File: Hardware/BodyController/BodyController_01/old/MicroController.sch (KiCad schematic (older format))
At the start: 18 parts, among them SW1 PTS645SM43SMTR92 LFS, U1 PIC33EPxxxMU810, Y1 8MHz

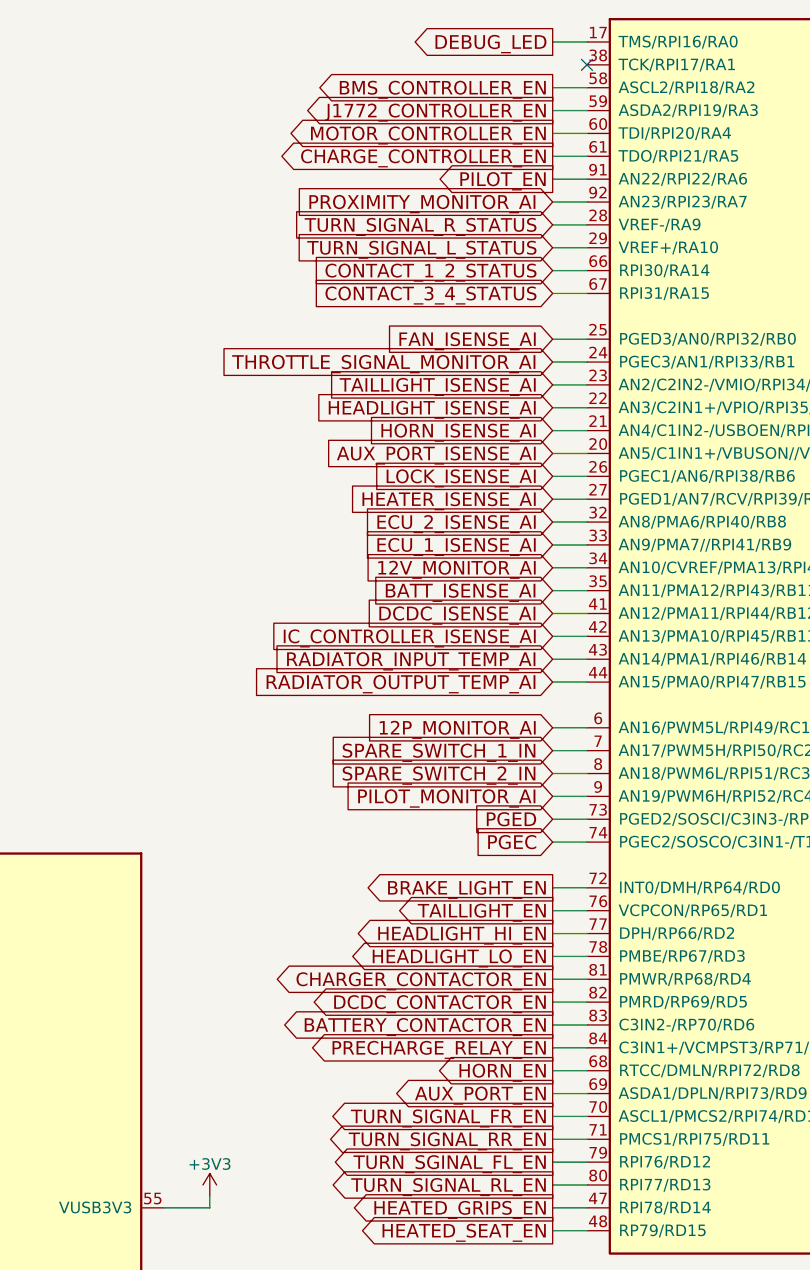
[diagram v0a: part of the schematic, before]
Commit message: Final layout for real this time. larger vias for EuroCircuit minimum rule.
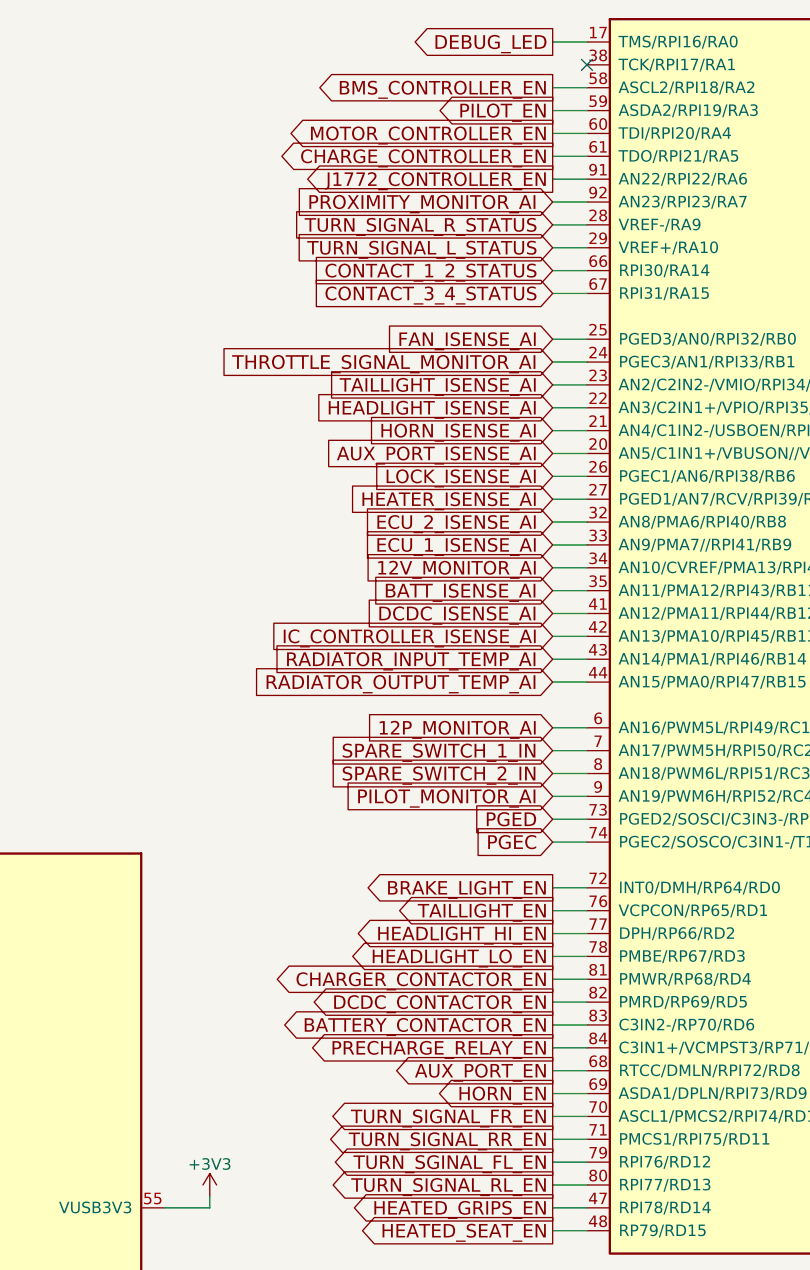
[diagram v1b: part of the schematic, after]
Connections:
- net AUX_PORT_EN: now also U1.68 (RTCC/DMLN/RPI72/RD8); no longer U1.69 (ASDA1/DPLN/RPI73/RD9)
- net HORN_EN: now also U1.69 (ASDA1/DPLN/RPI73/RD9); no longer U1.68 (RTCC/DMLN/RPI72/RD8)
- net J1772_CONTROLLER_EN: now also U1.91 (AN22/RPI22/RA6); no longer U1.59 (ASDA2/RPI19/RA3)
- net PILOT_EN: now also U1.59 (ASDA2/RPI19/RA3); no longer U1.91 (AN22/RPI22/RA6)
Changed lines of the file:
@@
 Text GLabel 5600 3000 0    59   Input ~ 0
 12V_MONITOR_AI
-Text GLabel 5600 5300 0    59   Output ~ 0
+Text GLabel 5600 5200 0    59   Output ~ 0
 AUX_PORT_EN
 Text GLabel 5600 4600 0    59   Output ~ 0
@@
 Text GLabel 5600 2200 0    59   Input ~ 0
 TAILLIGHT_ISENSE_AI
-Text GLabel 5600 5200 0    59   Output ~ 0
+Text GLabel 5600 5300 0    59   Output ~ 0
 HORN_EN
 Text GLabel 5600 2400 0    59   Input ~ 0
@@
 Text GLabel 10000 1300 2    59   Output ~ 0
 IC_CONTROLLER_SLEEP
-Text GLabel 5600 1000 0    59   Output ~ 0
+Text GLabel 5600 1300 0    59   Output ~ 0
 J1772_CONTROLLER_EN
 Text GLabel 10050 2450 2    60   Output ~ 0
@@
 Text GLabel 5600 1400 0    60   Input ~ 0
 PROXIMITY_MONITOR_AI
-Text GLabel 5600 1300 0    60   Output ~ 0
+Text GLabel 5600 1000 0    60   Output ~ 0
 PILOT_EN
 Wire Wire Line
